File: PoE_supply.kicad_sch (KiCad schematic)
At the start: 19 parts, among them Q1 PJE138K, U1 TPS2372-3RGWR, U4 IEA48003A280V-001-R

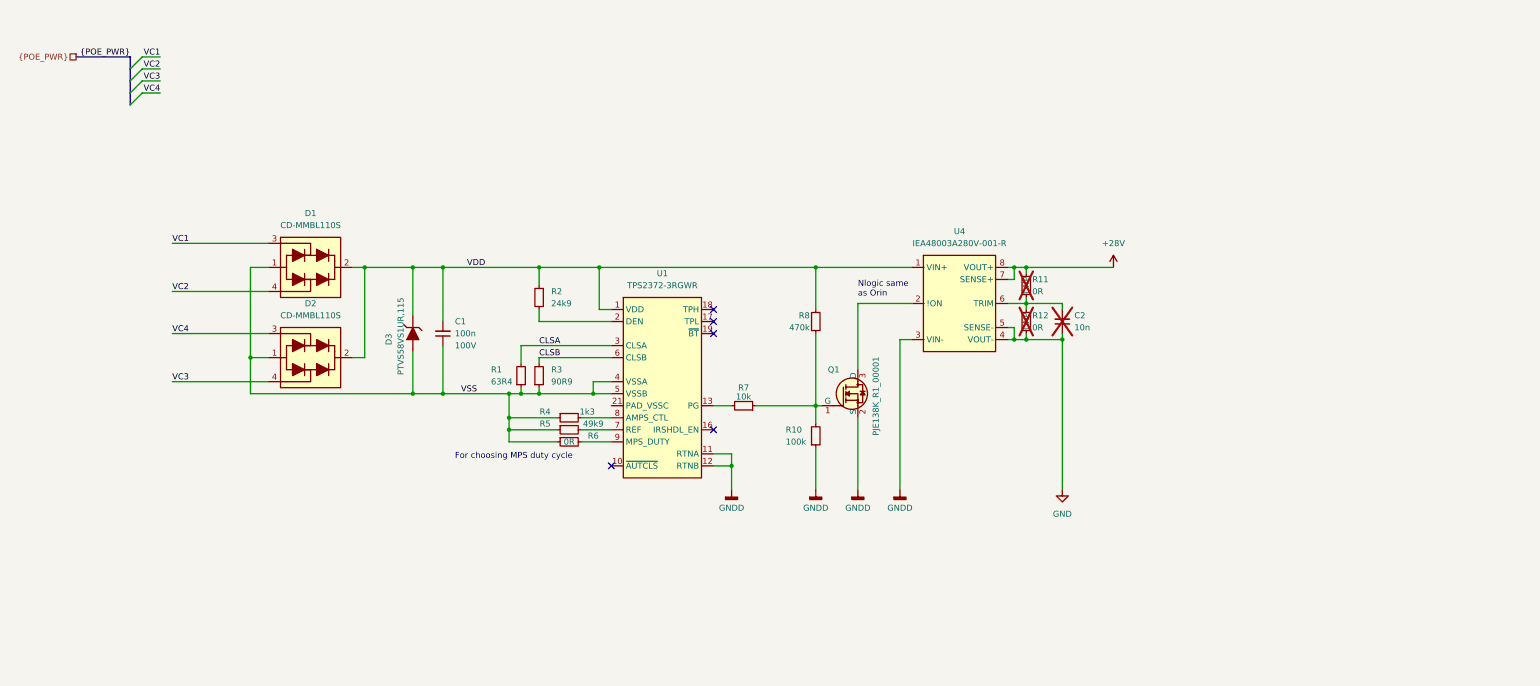
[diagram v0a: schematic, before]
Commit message: [#62623] Change hierarchy implementation
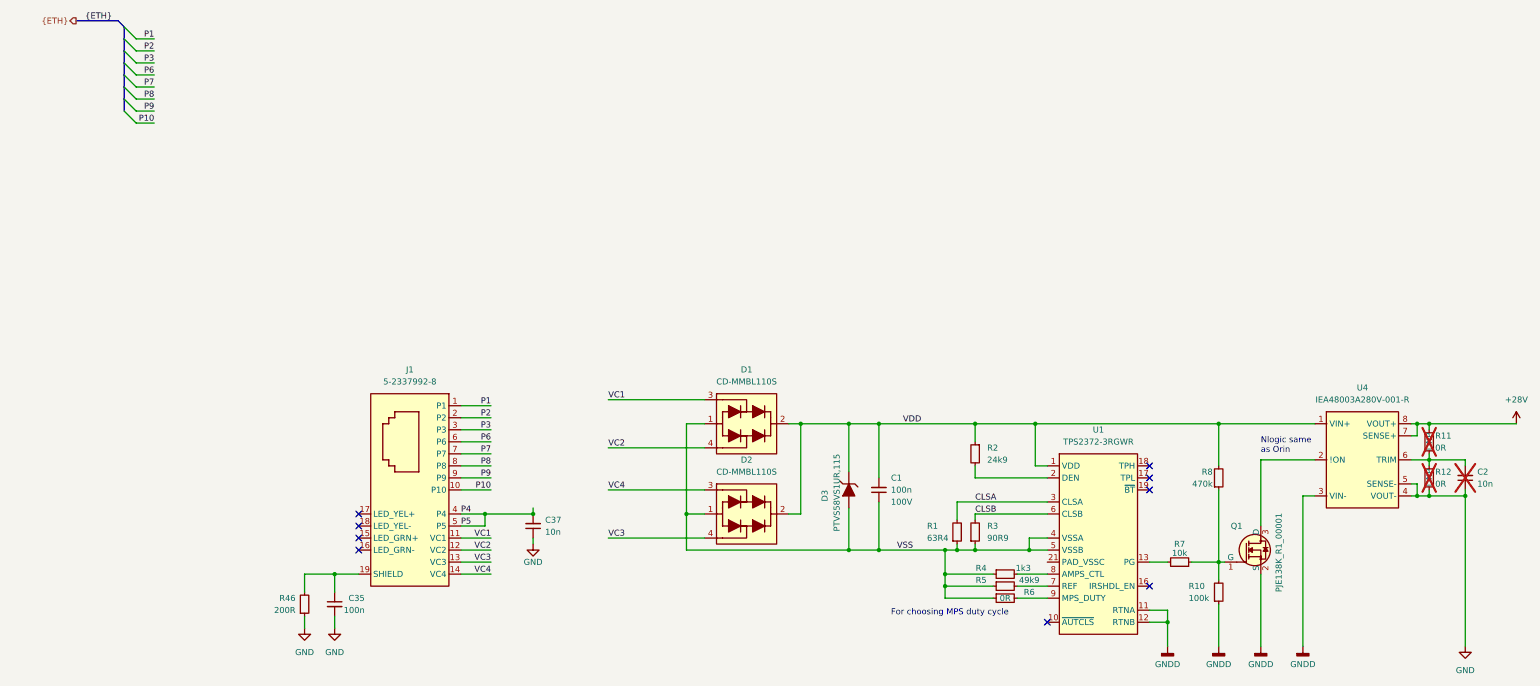
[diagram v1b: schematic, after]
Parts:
- added C35: C_100n_0402, antmicro-footprints:C_0402_1005Metric, symbol antmicroCapacitors0402:C_100n_0402
- added C37: C_10n_0603, antmicro-footprints:C_0603_1608Metric, symbol antmicroCapacitors0603:C_10n_0603
- added J1: Bus_RJ45_5-2337992-8, antmicro-footprints:RJ45_X-2337992-8_Horizontal, symbol antmicroModularConnectorsJacksWithMagnetics:Bus_RJ45_5-2337992-8
- added R46: R_200R_0402, antmicro-footprints:R_0402_1005Metric, symbol antmicroResistors0402:R_200R_0402
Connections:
- net GND: now also C35.2, C37.1, R46.1
- net VC1: now also J1.11 (VC1)
- net VC2: now also J1.12 (VC2)
- net VC3: now also J1.13 (VC3)
- net VC4: now also J1.14 (VC4)
- new net: C35.1, J1.19 (SHIELD), J1.20 (SHIELD), R46.2
- new net P1: J1.1 (P1)
- new net P10: J1.10 (P10)
- new net P2: J1.2 (P2)
- new net P3: J1.3 (P3)
- new net P4: C37.2, J1.4 (P4), J1.5 (P5)
- new net P6: J1.6 (P6)
- new net P7: J1.7 (P7)
- new net P8: J1.8 (P8)
- new net P9: J1.9 (P9)
- no-connect marks 5 -> 9
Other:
- moved on the sheet: C1, C2, D1, D2, D3, Q1, R1, R10, R11, R12, R2, R3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

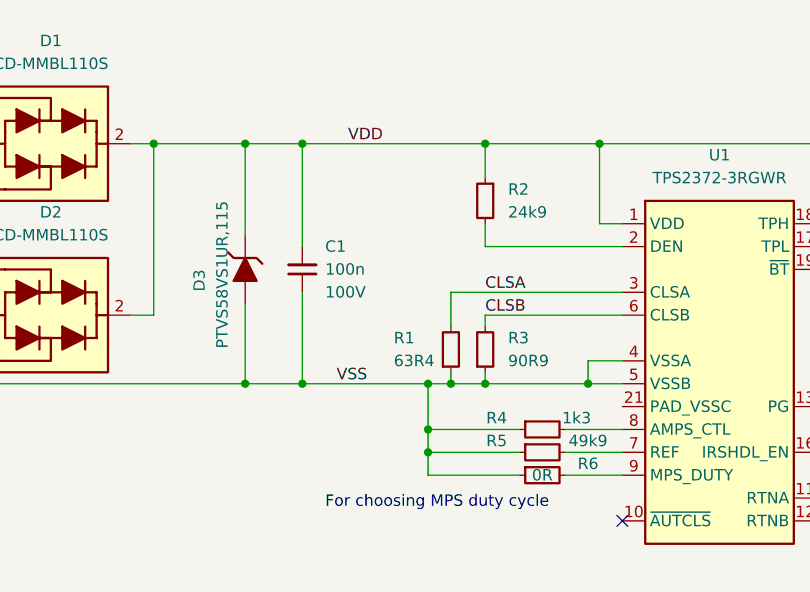
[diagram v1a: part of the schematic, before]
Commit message: [#62623] PCB initial placement
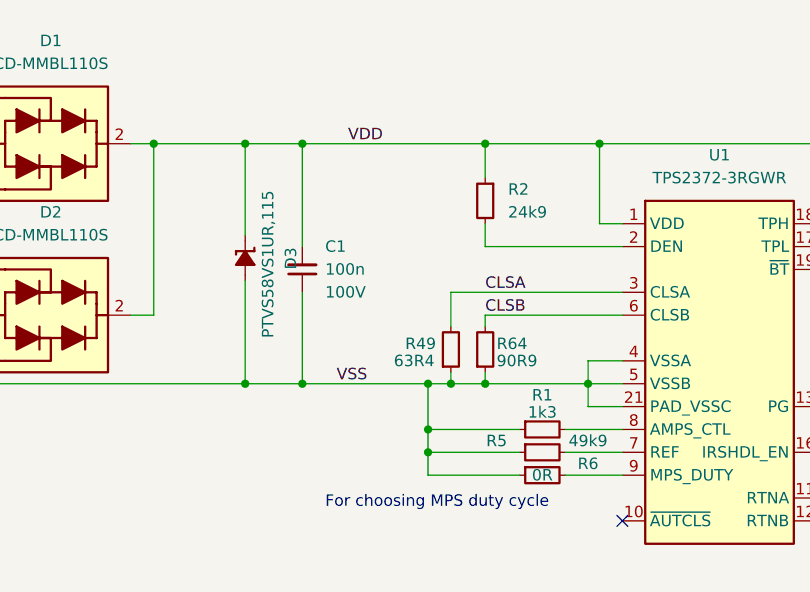
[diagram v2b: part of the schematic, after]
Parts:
- removed R1: R_63R4_0603, antmicro-footprints:R_0603_1608Metric, symbol antmicroResistors0603:R_63R4_0603
- removed R3: R_90R9_0603, antmicro-footprints:R_0603_1608Metric, symbol antmicroResistors0603:R_90R9_0603
- removed R4: R_1k3_0402, antmicro-footprints:R_0402_1005Metric, symbol antmicroResistors0402:R_1k3_0402
- added R1: R_1k3_0603, antmicro-footprints:R_0603_1608Metric, symbol antmicroResistors0603:R_1k3_0603
- added R49: R_63R4_0603, antmicro-footprints:R_0603_1608Metric, symbol antmicroResistors0603:R_63R4_0603
- added R64: R_90R9_0603, antmicro-footprints:R_0603_1608Metric, symbol antmicroResistors0603:R_90R9_0603
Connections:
- net CLSA: now also R49.2
- net CLSB: now also R64.2
- net VDD: now also D3.1 (C); no longer D3.K (C)
- net VSS: now also D3.2 (A), U1.21 (PAD_VSSC), R1.1, R49.1, R64.1; no longer D3.A
- net at U1.8 (AMPS_CTL): now also R1.2

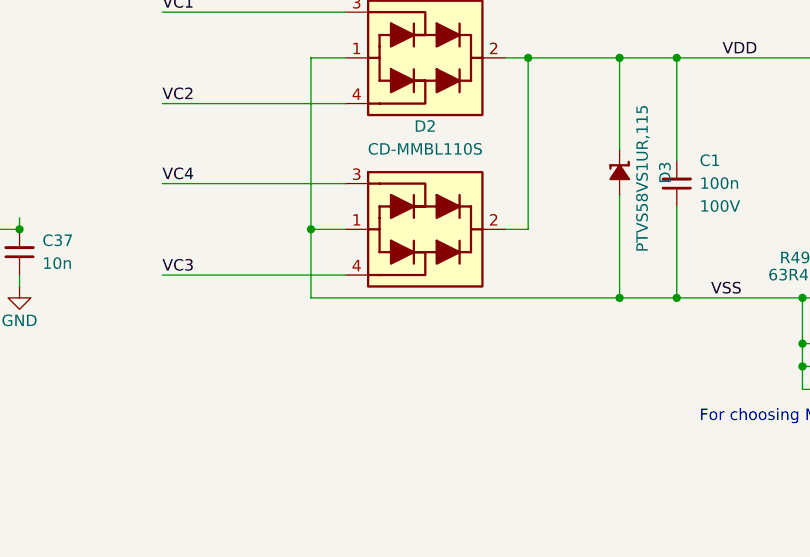
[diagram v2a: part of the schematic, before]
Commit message: [#62623] Add planes to variable buck
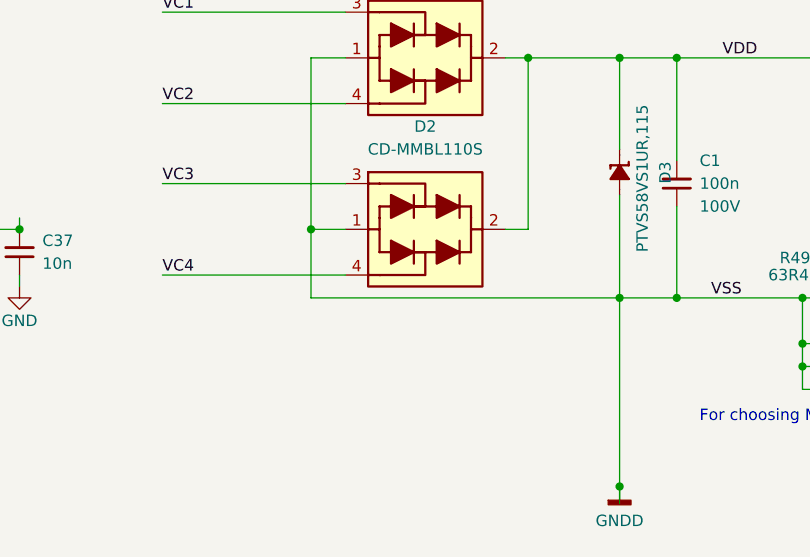
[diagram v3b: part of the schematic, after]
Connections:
- net VSS is gone; now on net GNDD: C1.1, D1.1, D2.1, D3.2 (A), R1.1, R49.1, R5.1, R6.1, R64.1, U1.21 (PAD_VSSC), U1.4 (VSSA), U1.5 (VSSB)
- net VC3: now also D2.3; no longer D2.4
- net VC4: now also D2.4; no longer D2.3
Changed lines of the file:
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@@
   (junction (at 320.04 123.19) (diameter 0) (color 0 0 0 0)
+  )
+  (junction (at 189.865 155.575) (diameter 0) (color 0 0 0 0)
   )
   (junction (at 267.97 137.16) (diameter 0) (color 0 0 0 0)
@@
     (stroke (width 0) (type default))
   )
+  (wire (pts (xy 189.865 155.575) (xy 189.865 157.48))
+    (stroke (width 0) (type default))
+  )
   (wire (pts (xy 212.725 133.35) (xy 212.725 134.62))
     (stroke (width 0) (type default))
@@
   )
   (wire (pts (xy 227.965 132.08) (xy 227.965 134.62))
+    (stroke (width 0) (type default))
+  )
+  (wire (pts (xy 189.865 134.62) (xy 189.865 155.575))
     (stroke (width 0) (type default))
   )
@@
     (effects (font (size 1.27 1.27)) (justify right bottom))
   )
-  (label "VC4" (at 139.065 121.92 0) (fields_autoplaced)
+  (label "VC4" (at 139.065 132.08 0) (fields_autoplaced)
     (effects (font (size 1.27 1.27)) (justify left bottom))
   )
@@
     (effects (font (size 1.27 1.27)) (justify right bottom))
   )
-  (label "VC3" (at 139.065 132.08 0) (fields_autoplaced)
+  (label "VC3" (at 139.065 121.92 0) (fields_autoplaced)
     (effects (font (size 1.27 1.27)) (justify left bottom))
   )
@@
         )
       )
+    )
+  )
+  (symbol (lib_id "antmicropower:GNDD") (at 189.865 155.575 0) (unit 1)
+    (in_bom yes) (on_board yes) (dnp no) (fields_autoplaced)
+    (property "Reference" "#PWR088" (at 205.105 158.115 0)
+      (effects (font (size 1.27 1.27) (thickness 0.15)) (justify left bottom) hide)
+    )
+    (property "Value" "GNDD" (at 189.865 159.385 0)
+      (effects (font (size 1.27 1.27) (thickness 0.15)))
+    )
+    (property "Footprint" "" (at 205.105 165.735 0)
+      (effects (font (size 1.27 1.27) (thickness 0.15)) (justify left bottom) hide)
+    )
+    (property "Datasheet" "" (at 205.105 168.275 0)
+      (effects (font (size 1.27 1.27) (thickness 0.15)) (justify left bottom) hide)
+    )
+    (property "Author" "Antmicro" (at 205.105 163.195 0)
+      (effects (font (size 1.27 1.27) (thickness 0.15)) (justify left bottom) hide)
+    )
+    (property "License" "Apache-2.0" (at 205.105 165.735 0)
+      (effects (font (size 1.27 1.27) (thickness 0.15)) (justify left bottom) hide)
+    )
+    (pin "1")
+    (instances
+      (project "antmicro-poe-to-usbc-pd-adapter"
+        (path "/cf0d4429-3f03-449f-96a7-26d69371a46d/a2b30c81-e263-4971-9235-45a28ceb7112"
+          (reference "#PWR088") (unit 1)
+        )
+      )

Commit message: [#62623] Las commit before major change in placement
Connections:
- net GNDD: no longer C1.1, D1.1, D2.1, D3.2 (A), R1.1, R49.1, R5.1, R6.1, R64.1, U1.21 (PAD_VSSC), U1.4 (VSSA), U1.5 (VSSB)
- new net VSS: C1.1, D1.1, D2.1, D3.2 (A), R1.1, R49.1, R5.1, R6.1, R64.1, U1.21 (PAD_VSSC), U1.4 (VSSA), U1.5 (VSSB)
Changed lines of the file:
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@@
   (junction (at 320.04 123.19) (diameter 0) (color 0 0 0 0)
-  )
-  (junction (at 189.865 155.575) (diameter 0) (color 0 0 0 0)
   )
   (junction (at 267.97 137.16) (diameter 0) (color 0 0 0 0)
@@
     (stroke (width 0) (type default))
   )
-  (wire (pts (xy 189.865 155.575) (xy 189.865 157.48))
-    (stroke (width 0) (type default))
-  )
   (wire (pts (xy 212.725 133.35) (xy 212.725 134.62))
     (stroke (width 0) (type default))
@@
   )
   (wire (pts (xy 227.965 132.08) (xy 227.965 134.62))
-    (stroke (width 0) (type default))
-  )
-  (wire (pts (xy 189.865 134.62) (xy 189.865 155.575))
     (stroke (width 0) (type default))
   )
@@
         )
       )
-    )
-  )
-  (symbol (lib_id "antmicropower:GNDD") (at 189.865 155.575 0) (unit 1)
-    (in_bom yes) (on_board yes) (dnp no) (fields_autoplaced)
-    (property "Reference" "#PWR088" (at 205.105 158.115 0)
-      (effects (font (size 1.27 1.27) (thickness 0.15)) (justify left bottom) hide)
-    )
-    (property "Value" "GNDD" (at 189.865 159.385 0)
-      (effects (font (size 1.27 1.27) (thickness 0.15)))
-    )
-    (property "Footprint" "" (at 205.105 165.735 0)
-      (effects (font (size 1.27 1.27) (thickness 0.15)) (justify left bottom) hide)
-    )
-    (property "Datasheet" "" (at 205.105 168.275 0)
-      (effects (font (size 1.27 1.27) (thickness 0.15)) (justify left bottom) hide)
-    )
-    (property "Author" "Antmicro" (at 205.105 163.195 0)
-      (effects (font (size 1.27 1.27) (thickness 0.15)) (justify left bottom) hide)
-    )
-    (property "License" "Apache-2.0" (at 205.105 165.735 0)
-      (effects (font (size 1.27 1.27) (thickness 0.15)) (justify left bottom) hide)
-    )
-    (pin "1")
-    (instances
-      (project "antmicro-poe-to-usbc-pd-adapter"
-        (path "/cf0d4429-3f03-449f-96a7-26d69371a46d/a2b30c81-e263-4971-9235-45a28ceb7112"
-          (reference "#PWR088") (unit 1)
-        )
-      )
